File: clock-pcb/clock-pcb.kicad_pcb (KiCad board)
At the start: 2 copper layers, 66 x 42 mm, 61 parts, among them J1 Conn_01x03_Pin, J10 Conn_01x01_Socket, J11 Conn_01x01_Socket, J12 Conn_01x01_Socket, J13 Conn_01x01_Socket, J14 Conn_01x01_Socket, J15 Conn_01x02_Socket, J2 oled, J3 Led display, J4 Led display 2, J5 Conn_01x07_Socket, J6 Conn_01x07_Socket, J7 Conn_01x01_Socket, J8 Conn_01x02_Socket, J9 Conn_01x01_Socket, Q1 FS8205A, Q2 FDN304PZ, U1 ESP32-WROOM-E, U4 TPS2116DRL, U5 MCP73811T-420I-OT, U7 TLV75533PDBV

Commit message: new pcb
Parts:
- removed BATT_P1, BOOT1, EN1: TL3305AF160QG, clock:TL3305AF160QG
- removed D4: SD0805S040S0R5, Diode_SMD:D_0805_2012Metric
- removed J11, J12, J13, J14: Conn_01x01_Socket, Connector_PinSocket_2.54mm:PinSocket_1x01_P2.54mm_Vertical
- removed JP3: Jumper_bridged, Jumper:SolderJumper-2_P1.3mm_Bridged2Bar_RoundedPad1.0x1.5mm
- removed JP4: SolderJumper_3_Open, Jumper:SolderJumper-3_P1.3mm_Open_RoundedPad1.0x1.5mm
- removed Q1: FS8205A, clock:SOP65P640X120-8N
- removed Q2: FDN304PZ, Package_TO_SOT_SMD:SOT-23
- removed USB_BOARD1: Conn_01x02_Socket, clock:SHDR2W64P0X250_1X2_740X575X700P
- added C12: 1uF, Capacitor_SMD:C_0603_1608Metric, B.Cu at (93.0, 135.5)
- added C13: 1uF, Capacitor_SMD:C_0603_1608Metric, B.Cu at (99.5, 151.8)
- added C14: 1uF, Capacitor_SMD:C_0603_1608Metric, B.Cu at (98.0, 132.4)
- added C15: 1uF, Capacitor_SMD:C_0603_1608Metric, B.Cu at (106.8, 130.1)
- added C16: 4.7uF, Capacitor_SMD:C_0805_2012Metric, B.Cu at (87.5, 152.0)
- added C17: 10uF, Capacitor_SMD:C_0603_1608Metric, B.Cu at (93.9, 155.9)
- added C18: 6.4pF, Capacitor_SMD:C_0402_1005Metric, B.Cu at (92.4, 155.3)
- added C19: 19pF, Capacitor_SMD:C_0402_1005Metric, B.Cu at (91.9, 147.8)
- added C20: 19pF, Capacitor_SMD:C_0402_1005Metric, B.Cu at (91.9, 149.7)
- added C21: 1uF, Capacitor_SMD:C_0603_1608Metric, B.Cu at (89.2, 152.0)
- added C23: 0.1uF, Capacitor_SMD:C_0603_1608Metric, B.Cu at (105.0, 151.9)
- added C24: 10uF, Capacitor_SMD:C_0603_1608Metric, B.Cu at (105.0, 153.4)
- added C25: 1uF, Capacitor_SMD:C_0603_1608Metric, B.Cu at (100.8, 154.0)
- added C26: 4.7uF, Capacitor_Tantalum_SMD:CP_EIA-3528-12_Kemet-T, B.Cu at (93.3, 152.6)
- added C27: 4.7uF, Capacitor_Tantalum_SMD:CP_EIA-3528-12_Kemet-T, B.Cu at (111.5, 153.6)
- added C28: 1uF, Capacitor_SMD:C_0603_1608Metric, B.Cu at (97.6, 154.0)
- added D1: LED, LED_SMD:LED_1210_3225Metric, F.Cu at (82.9, 154.9)
- added D2: LED, LED_SMD:LED_1210_3225Metric, F.Cu at (82.9, 131.3)
- added IC2: MCP23018-E_MJ, clock:QFN50P400X400X90-25N-D, B.Cu at (90.7, 140.4)
- added JP6: Jumper, clock:jumper_solder_small, B.Cu at (99.2, 134.3)
- added L1: 10uH 1A, clock:HPI0530-100, B.Cu at (87.8, 160.0)
- added R0: 5.1k, Resistor_SMD:R_0402_1005Metric, B.Cu at (94.9, 140.5)
- added R13: 250k, Resistor_SMD:R_0402_1005Metric, B.Cu at (118.5, 135.5)
- added R14: 100k, Resistor_SMD:R_0402_1005Metric, B.Cu at (119.3, 133.6)
- added R15: 10K, Resistor_SMD:R_0402_1005Metric, B.Cu at (107.0, 126.6)
- added R16: 10K, Resistor_SMD:R_0402_1005Metric, B.Cu at (109.6, 126.6)
- added R17: 330, Resistor_SMD:R_0402_1005Metric, F.Cu at (86.2, 153.2)
- added R18: 330, Resistor_SMD:R_0402_1005Metric, F.Cu at (86.2, 156.6)
- added R19: 330, Resistor_SMD:R_0402_1005Metric, F.Cu at (86.2, 154.0)
- added R20: 330, Resistor_SMD:R_0402_1005Metric, F.Cu at (86.2, 155.8)
- added R21: 10M, Resistor_SMD:R_0402_1005Metric, B.Cu at (95.3, 148.6)
- added R22: 330, Resistor_SMD:R_0402_1005Metric, F.Cu at (86.2, 132.2)
- added R23: 330, Resistor_SMD:R_0402_1005Metric, F.Cu at (86.2, 133.0)
- added R24: 330, Resistor_SMD:R_0402_1005Metric, F.Cu at (86.2, 130.4)
- added R25: 330, Resistor_SMD:R_0402_1005Metric, F.Cu at (86.2, 129.6)
- added R26: 300k, Resistor_SMD:R_0402_1005Metric, B.Cu at (91.8, 156.9)
- added R27: 3.16M, Resistor_SMD:R_0402_1005Metric, B.Cu at (91.4, 155.3)
- added R29: 1.2M, Resistor_SMD:R_0402_1005Metric, B.Cu at (103.0, 154.0)
- added R30: 10K, Resistor_SMD:R_0402_1005Metric, B.Cu at (108.3, 153.0)
- added R31: 10K, Resistor_SMD:R_0402_1005Metric, B.Cu at (107.3, 153.0)
- added R32: N/A, Resistor_SMD:R_0402_1005Metric, B.Cu at (99.0, 136.0)
- added R33: N/A, Resistor_SMD:R_0402_1005Metric, B.Cu at (97.7, 136.0)
- added S1: TS21-34-035-BK-160-SMT-TR, clock:TS2134035BK160SMTTR, F.Cu at (142.4, 160.9)
- added S2: TS21-34-035-BK-160-SMT-TR, clock:TS2134035BK160SMTTR, F.Cu at (142.4, 155.4)
- added S5: TS21-34-035-BK-160-SMT-TR, clock:TS2134035BK160SMTTR, F.Cu at (133.5, 149.3)
- added TP1: TestPoint, TestPoint:TestPoint_THTPad_1.0x1.0mm_Drill0.5mm, F.Cu at (81.5, 127.5)
- added TP12: TestPoint, TestPoint:TestPoint_THTPad_1.0x1.0mm_Drill0.5mm, F.Cu at (90.3, 124.7)
- added TP13: TestPoint, TestPoint:TestPoint_THTPad_1.0x1.0mm_Drill0.5mm, F.Cu at (94.7, 124.7)
- added TP3: TestPoint, TestPoint:TestPoint_THTPad_1.0x1.0mm_Drill0.5mm, F.Cu at (83.6, 124.7)
- added TP4: TestPoint, TestPoint:TestPoint_THTPad_1.0x1.0mm_Drill0.5mm, F.Cu at (81.4, 124.7)
- added TP5: TestPoint, TestPoint:TestPoint_THTPad_1.0x1.0mm_Drill0.5mm, F.Cu at (88.0, 124.7)
- added TP6: TestPoint, TestPoint:TestPoint_THTPad_1.0x1.0mm_Drill0.5mm, F.Cu at (85.8, 124.7)
- added TP7: TestPoint, TestPoint:TestPoint_THTPad_1.0x1.0mm_Drill0.5mm, F.Cu at (92.5, 124.7)
- added TP8: TestPoint, TestPoint:TestPoint_THTPad_1.0x1.0mm_Drill0.5mm, F.Cu at (96.9, 124.7)
- added TP9: TestPoint, TestPoint:TestPoint_THTPad_1.0x1.0mm_Drill0.5mm, F.Cu at (83.8, 127.5)
- added U6: TPS61040DBV, Package_TO_SOT_SMD:SOT-23-5, B.Cu at (88.6, 155.7)
- added U8: AT42QT2120-MMHR, clock:QFN45P300X300X85-21N, B.Cu at (102.1, 129.4)
- added Y2: 32.768KHz, clock:XTAL_9HT10_TXC, B.Cu at (93.6, 148.6)
- C1: value 22uF -> 0.1uF; footprint Capacitor_SMD:C_0805_2012Metric -> Capacitor_SMD:C_0603_1608Metric
- C10, C11, U5: moved to B.Cu
- C3: value 0.1uF -> 10uF
- D3: value SD0805S040S0R5 -> NSVR0340HT1G; footprint Diode_SMD:D_0805_2012Metric -> Diode_SMD:D_SOD-323
- J10: value Conn_01x01_Socket -> Conn_01x05_Socket; footprint Connector_PinSocket_2.54mm:PinSocket_1x01_P2.54mm_Vertical -> Connector_PinHeader_2.54mm:PinHeader_1x05_P2.54mm_Vertical
- J2: value oled -> oled 2
- J5, J6: footprint Connector_PinSocket_2.54mm:PinSocket_1x07_P2.54mm_Vertical -> Connector_PinHeader_2.54mm:PinHeader_1x07_P2.54mm_Vertical
- J7: value Conn_01x01_Socket -> SFV25R-2STE1HLF; footprint Connector_PinSocket_2.54mm:PinSocket_1x01_P2.54mm_Vertical -> clock:OLED_1.5IN_128X128MONO; moved to F.Cu
- J8: value Conn_01x02_Socket -> SFV25R-2STE1HLF; footprint Connector_PinSocket_2.54mm:PinSocket_1x02_P2.54mm_Vertical -> clock:AMPHENOL_SFV25R-2STE1HLF
- J9: value Conn_01x01_Socket -> Conn_01x04_Socket; footprint Connector_PinSocket_2.54mm:PinSocket_1x01_P2.54mm_Vertical -> Connector_JST:JST_XH_B4B-XH-AM_1x04_P2.50mm_Vertical
- JP1, JP7: footprint Jumper:SolderJumper-2_P1.3mm_Open_RoundedPad1.0x1.5mm -> clock:jumper_solder_small
- JP2: value Jumper -> SolderJumper_3_Bridged12; footprint Jumper:SolderJumper-2_P1.3mm_Open_RoundedPad1.0x1.5mm -> clock:jumper_solder_small_3_bridged
- JP5: value SolderJumper_2_Open -> Jumper; footprint Jumper:SolderJumper-2_P1.3mm_Open_RoundedPad1.0x1.5mm -> clock:jumper_solder_small; moved to B.Cu
- R1: value 10k -> 100k
- R10: value 800k -> 10K
- R11: value 5.1k -> 10K
- R12: value 5.1k -> 100k
- R7: value 500k -> 47K
- R8: value 100K -> 10K
- R9: value 50k -> 10K
- U1: value ESP32-WROOM-E -> ESP32-C6-MINI-1-N4; footprint PCM_Espressif:ESP32-WROOM-32E -> clock:XCVR_ESP32-C6-MINI-1-N4
- U3: footprint clock:SHDR2W64P0X250_1X2_740X575X700P -> Connector_JST:JST_XH_B2B-XH-AM_1x02_P2.50mm_Vertical
- moved J8 37.8 mm to (104.5, 158.7), turned to 180 degrees
- moved J9 29.8 mm to (122.9, 146.8)
- moved C1 28.6 mm to (105.1, 130.1), turned to 90 degrees
- moved D3 28.0 mm to (92.5, 159.4)
- moved R8 25.4 mm to (99.4, 126.6), turned to -90 degrees
- moved R10 25.2 mm to (105.0, 126.6)
- moved R9 24.6 mm to (102.9, 126.3), turned to -90 degrees
- moved R7 23.8 mm to (98.9, 131.0), turned to 0 degrees
- moved JP5 22.7 mm to (97.4, 134.3), turned to 0 degrees
- moved R1 22.3 mm to (106.0, 134.7), turned to 90 degrees
- moved C2 20.4 mm to (89.8, 135.5), turned to 90 degrees
- moved JP2 19.7 mm to (101.2, 126.3), turned to 180 degrees
- moved R11 17.8 mm to (101.9, 152.1), turned to 180 degrees
- moved C3 17.2 mm to (91.3, 135.5), turned to 90 degrees
- moved J7 16.6 mm to (104.5, 144.4), turned to 0 degrees
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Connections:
- net CO renamed Net-(AO9926C1-G2)
- net DO renamed Net-(AO9926C1-G1)
- C1 pad 1: +3V3 -> GND
- C1 pad 2: GND -> +3V3
- C3 pad 1: GND -> +3V3
- C3 pad 2: EN -> GND
- D3 pad 1: Net-(D3-K) -> 14V_OLED
- D3 pad 2: VBUS -> Net-(D3-A)
- J2 pad 1: +3V3 -> GND
- J2 pad 2: GND -> +3V3
- J3 pad 1: CLK -> SCL
- J3 pad 2: DIO -> SDA
- J4 pad 1: GND -> CLK
- J4 pad 2: +3V3 -> DIO
- J4 pad 3: DIO -> GND
- J4 pad 4: CLK -> +3V3
- J5 pad 3: GPIO35 -> SUB_TOP_3
- J5 pad 4: GPIO14 -> BUZZER
- J5 pad 5: GPIO15 -> SUB_TOP_1
- J6 pad 3: GPIO39 -> HALL_SENS
- J6 pad 4: GPIO26 -> BUTTON_EXIT
- J6 pad 5: GPIO25 -> BUTON_CONF
- J7 pad 1: Net-(J7-Pin_1) -> GND
- J8 pad 2: GPIO4_T -> 14V_OLED
- J9 pad 1: Net-(J9-Pin_1) -> GND
- JP2 pad 1: GND -> Net-(JP2-A)
- JP2 pad 2: Net-(JP2-B) -> GUARD
- JP5 pad 1: GND -> SDA
- JP5 pad 2: CHARGE_EN -> MOSI
- R1 pad 2: EN -> SCL
- R10 pad 1: POWER_STATUS -> Net-(J10-Pin_3)
- R10 pad 2: GND -> SLID_1
- R11 pad 2: SCL -> EN
- R2 pad 2: ADC_BATT -> ADC
- R3 pad 1: ADC_BATT -> ADC
- R7 pad 1: VBUS -> +3V3
- R7 pad 2: POWER_STATUS -> TOUCH_INT
- R8 pad 1: Net-(D3-K) -> Net-(J10-Pin_5)
- R8 pad 2: GND -> SLID_0
- R9 pad 1: VBUS -> Net-(J10-Pin_4)
- R9 pad 2: GND -> GUARD
- S3 pad 1: GND -> +3V3
- S3 pad 2: GND -> +3V3
- S4 pad 1: GND -> +3V3
- S4 pad 2: GND -> +3V3
- U1 pad 10: GPIO25 -> INT_A
- U1 pad 11: GPIO26 -> GND
- U1 pad 12: Net-(J11-Pin_1) -> CLOCK_P
- U1 pad 13: GPIO14 -> CLOCK_N
- U1 pad 14: BUTTON_UP -> GND
- U1 pad 15: GND -> SDA
- U1 pad 16: BUTTON_DOWN -> SCL
- U1 pad 17: (no net) -> DN
- U1 pad 18: (no net) -> DP
- U1 pad 19: (no net) -> CLK
- U1 pad 2: +3V3 -> GND
- U1 pad 20: (no net) -> DIO
- U1 pad 21: (no net) -> unconnected-(U1-NC__2-Pad21)
- U1 pad 22: (no net) -> Net-(U1-IO8)
- U1 pad 23: GPIO15 -> GPIO9
- U1 pad 24: Net-(J10-Pin_1) -> BUZZER
- U1 pad 25: IO0 -> Net-(U1-IO19)
- U1 pad 26: GPIO4_T -> Net-(U1-IO20)
- U1 pad 27: Net-(J12-Pin_1) -> DC
- U1 pad 28: Net-(J13-Pin_1) -> CS
- U1 pad 29: Net-(J9-Pin_1) -> Net-(U1-IO23)
- U1 pad 3: EN -> +3V3
- U1 pad 30: CLK -> RX
- U1 pad 31: DIO -> TX
- U1 pad 32: (no net) -> unconnected-(U1-NC__3-Pad32)
- U1 pad 33: SDA -> unconnected-(U1-NC__4-Pad33)
- U1 pad 34: RX -> unconnected-(U1-NC__5-Pad34)
- U1 pad 35: TX -> unconnected-(U1-NC__6-Pad35)
- U1 pad 36: SCL -> GND
- U1 pad 37: CHARGE_EN -> GND
- U1 pad 4: POWER_STATUS -> unconnected-(U1-NC-Pad4)
- U1 pad 5: GPIO39 -> Net-(U1-IO2)
- U1 pad 6: ADC_BATT -> TOUCH_INT
- U1 pad 7: GPIO35 -> unconnected-(U1-NC__1-Pad7)
- U1 pad 8: Net-(J7-Pin_1) -> EN
- U1 pad 9: Net-(J14-Pin_1) -> ADC
- U4 pad 4: Net-(JP2-B) -> Net-(U4-PR1)
- U5 pad 5: Net-(JP4-C) -> GND
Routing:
- net +3V3: track 112.3 -> 0.00 mm, vias 2 -> 0
- net SCL: track 112.2 -> 0.00 mm, vias 2 -> 0
- net SDA: track 97.0 -> 0.00 mm, vias 1 -> 0
- net GPIO35: track 65.5 -> 0.00 mm
- net GPIO39: track 61.0 -> 0.00 mm, vias 1 -> 0
- net GPIO25: track 55.6 -> 0.00 mm, vias 1 -> 0
- net GPIO26: track 54.3 -> 0.00 mm, vias 1 -> 0
- net POWER_STATUS: track 50.5 -> 0.00 mm
- net GPIO14: track 49.9 -> 0.00 mm, vias 2 -> 0
- net BUTTON_UP: track 49.5 -> 0.00 mm, vias 1 -> 0
- net GND: track 48.2 -> 0.00 mm, vias 202 -> 0
- net BUTTON_DOWN: track 46.1 -> 0.00 mm, vias 2 -> 0
- net LDO_IN: track 44.5 -> 0.00 mm
- net +BATT: track 43.4 -> 0.00 mm, vias 1 -> 0
- net Net-(J9-Pin_1): track 38.0 -> 0.00 mm, vias 3 -> 0
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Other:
- outline, holes or cut-outs redrawn
- board text removed: "GPIO16"
- board text removed: "GPIO17"
- board text removed: "GPIO2"
- board text removed: "GPIO27"
- board text removed: "GPIO32"
- board text removed: "GPIO33"
- board text removed: "GPIO4_T"
- board text removed: "GPIO5"

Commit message: routing
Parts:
- R2, R3, S5: moved to B.Cu
- moved R2 5.06 mm to (117.5, 152.7)
- moved R3 5.06 mm to (115.5, 152.7)
- moved TP8 4.45 mm to (92.5, 124.7)
- moved TP12 4.44 mm to (94.7, 124.7)
- moved TP3 2.24 mm to (81.4, 124.7)
- moved TP5 2.24 mm to (85.8, 124.7)
- moved TP7 2.23 mm to (90.3, 124.7)
- moved TP13 2.22 mm to (96.9, 124.7)
- moved TP6 2.21 mm to (88.0, 124.7)
- moved TP4 2.21 mm to (83.6, 124.7)
- moved S2 1.03 mm to (143.4, 155.6)
- moved S1 1.03 mm to (143.4, 161.1)
- moved JP1 0.40 mm to (128.4, 155.0)
- moved J8 0.40 mm to (104.5, 159.1)
- moved R14 0.25 mm to (119.1, 133.8)
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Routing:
- net +3V3: track 0.00 -> 253.5 mm, vias 0 -> 9
- net GND: track 0.00 -> 155.3 mm, vias 0 -> 127
- net SDA: track 0.00 -> 133.0 mm, vias 0 -> 6
- net EN: track 0.00 -> 128.3 mm, vias 0 -> 11
- net SCL: track 0.00 -> 122.0 mm, vias 0 -> 4
- net SUB_TOP_1: track 0.00 -> 114.5 mm, vias 0 -> 6
- net SUB_TOP_3: track 0.00 -> 112.7 mm, vias 0 -> 6
- net GPIO9: track 0.00 -> 73.4 mm, vias 0 -> 3
- net BUTTON_EXIT: track 0.00 -> 69.3 mm, vias 0 -> 3
- net BUTTON_DOWN: track 0.00 -> 58.6 mm, vias 0 -> 3
- net BUTON_CONF: track 0.00 -> 56.2 mm, vias 0 -> 1
- net BUZZER: track 0.00 -> 56.1 mm, vias 0 -> 2
- net BUTTON_UP: track 0.00 -> 53.4 mm, vias 0 -> 3
- net TOUCH_INT: track 0.00 -> 51.9 mm, vias 0 -> 4
- net Net-(U1-IO2): track 0.00 -> 50.2 mm, vias 0 -> 2
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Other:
- outline, holes or cut-outs redrawn
- board text added: "BOOT"
- board text added: "EN"
- board text removed: "3.3V"
- board text removed: "GND"

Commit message: touch slider pcb
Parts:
- removed J10: Conn_01x05_Socket, Connector_PinHeader_2.54mm:PinHeader_1x05_P2.54mm_Vertical
- added J11: Conn_01x06_Socket, Connector_PinHeader_2.54mm:PinHeader_1x06_P2.54mm_Vertical, B.Cu at (112.1, 124.2)
- added R28: 10K, Resistor_SMD:R_0402_1005Metric, B.Cu at (139.8, 149.3)
- moved R15 34.2 mm to (139.8, 136.6)
- moved TP12 0.49 mm to (94.7, 124.2)
- moved TP13 0.49 mm to (96.9, 124.2)
- moved TP3 0.49 mm to (81.4, 124.2)
- moved TP4 0.49 mm to (83.6, 124.2)
- moved TP5 0.49 mm to (85.8, 124.2)
- moved TP6 0.49 mm to (88.0, 124.2)
- moved TP7 0.49 mm to (90.3, 124.2)
- moved TP8 0.49 mm to (92.5, 124.2)
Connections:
- JP2 pad 1: Net-(JP2-A) -> GUARD
- R15 pad 1: Net-(J10-Pin_2) -> BUTTON_UP
- R15 pad 2: GUARD -> +3V3
- R16 pad 2: SLID_1 -> SLID_0
- R8 pad 2: SLID_0 -> SLID_2
- S3 pad 1: +3V3 -> GND
- S3 pad 2: +3V3 -> GND
- S4 pad 1: +3V3 -> GND
- S4 pad 2: +3V3 -> GND
- U8 pad 4: Net-(JP2-A) -> GUARD
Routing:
- net GND: track 155.3 -> 189.2 mm, vias 127 -> 131
- net +3V3: track 253.5 -> 222.2 mm, vias 9 -> 11
- net Net-(J11-Pin_1): track 1.80 -> 13.2 mm
- net SLID_1: track 8.45 -> 1.99 mm, vias 2 -> 0
- net SLID_2: track 0.00 -> 6.31 mm, vias 0 -> 2
- net SLID_0: track 11.0 -> 6.75 mm, vias 2 -> 0
- net SCL: track 122.0 -> 119.9 mm
- net BUTTON_UP: track 53.4 -> 55.5 mm
- net Net-(JP2-A): track 1.94 -> 0.00 mm
- net BUTTON_DOWN: track 58.6 -> 60.4 mm
- net Net-(J10-Pin_2): track 1.74 -> 0.00 mm
- net GUARD: track 7.67 -> 6.90 mm
- net SDA: track 133.0 -> 132.4 mm
- net Net-(U8-KEY4/GPO2): track 7.71 -> 8.22 mm

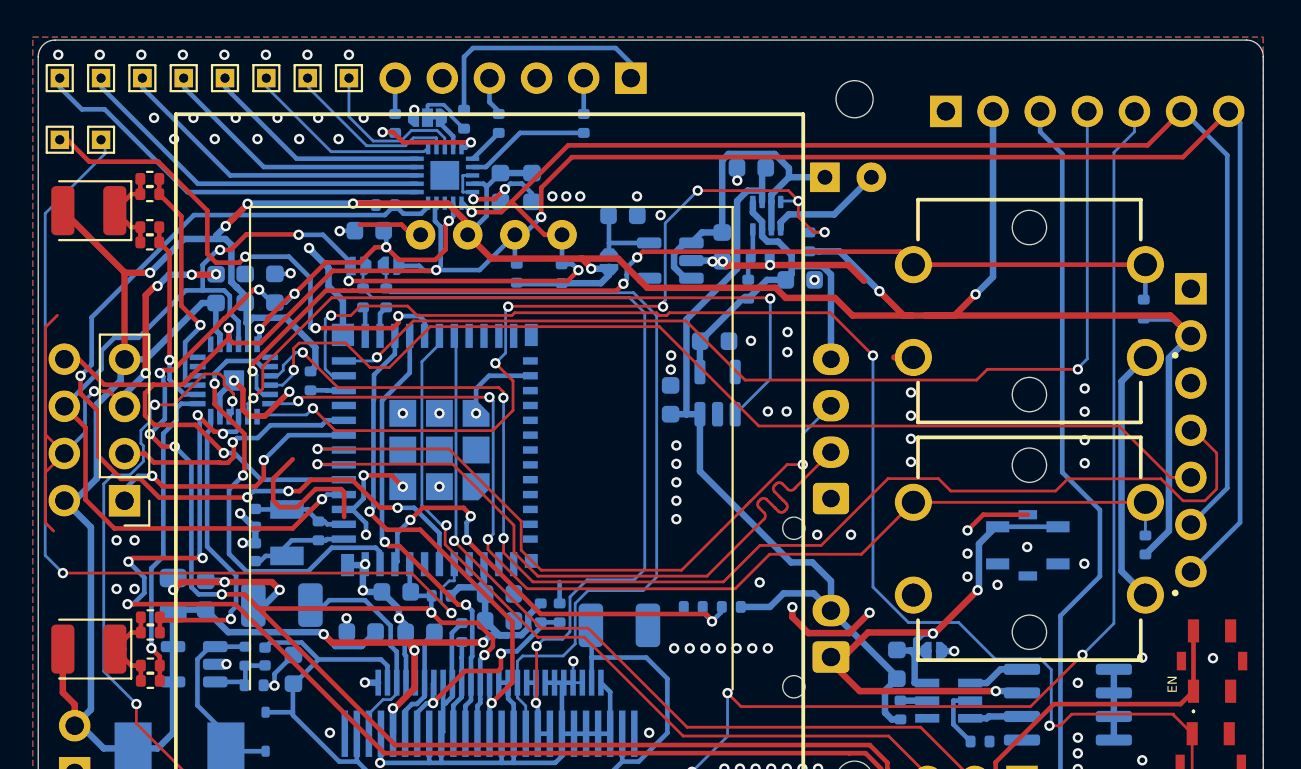
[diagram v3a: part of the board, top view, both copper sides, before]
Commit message: voltage regulator
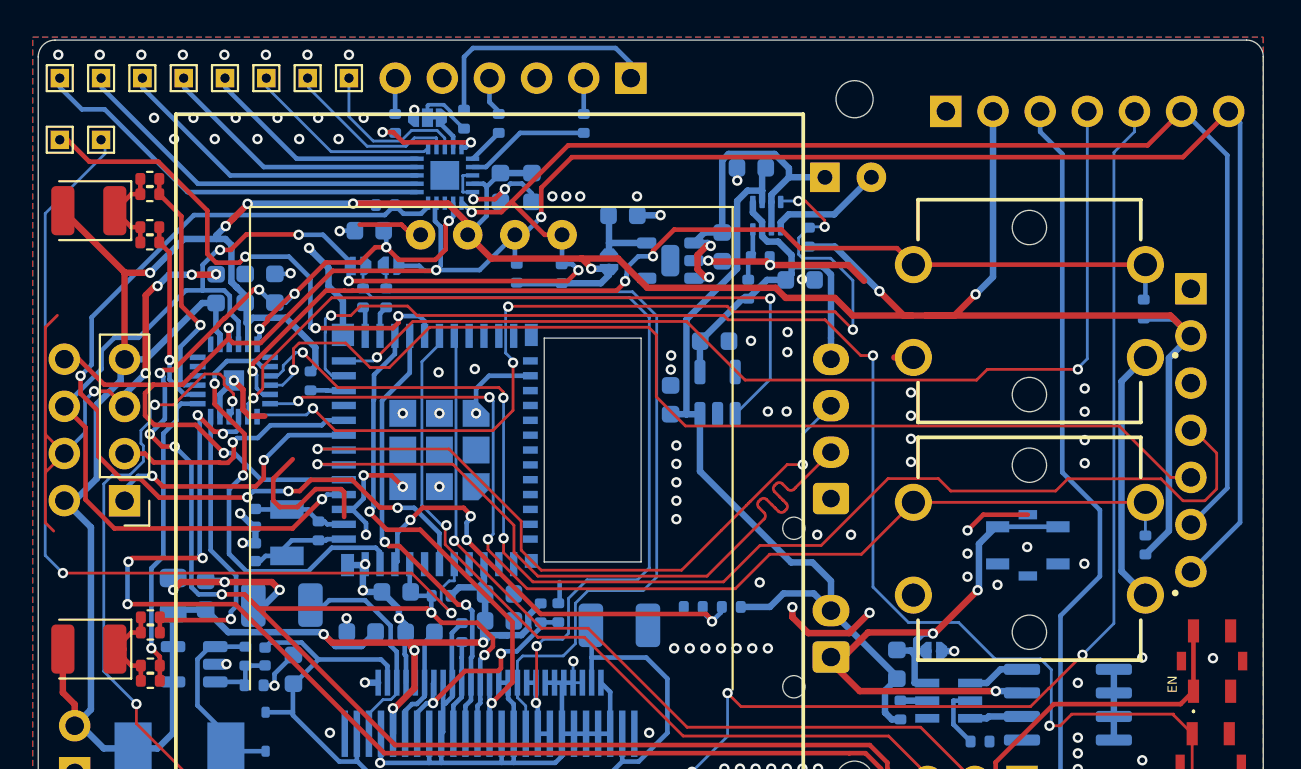
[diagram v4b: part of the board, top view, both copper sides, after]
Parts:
- U7: footprint Package_TO_SOT_SMD:SOT-23-5 -> clock:TLV75733PDYDR
- moved R6 0.26 mm to (121.7, 132.7)
- moved R30 0.07 mm to (108.2, 153.0)
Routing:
- net POWER_STATUS: track 46.7 -> 51.7 mm, vias 7 -> 6
- net BUTON_CONF: track 56.2 -> 58.1 mm
- net BUTTON_UP: track 55.5 -> 56.7 mm
- net LDO_IN: track 18.5 -> 19.6 mm, vias 0 -> 2
- net SUB_TOP_3: track 112.7 -> 111.9 mm
- net GND: track 189.2 -> 189.3 mm, vias 131 -> 127
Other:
- outline, holes or cut-outs redrawn

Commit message: panel
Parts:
- added C22: 6.4pF, Capacitor_SMD:C_01005_0402Metric, B.Cu at (93.4, 155.5)
- added TP10: TestPoint, TestPoint:TestPoint_THTPad_1.0x1.0mm_Drill0.5mm, F.Cu at (85.8, 127.5)
- added TP2: TestPoint, TestPoint:TestPoint_Pad_D1.0mm, B.Cu at (93.8, 161.4)
- J4: footprint Connector_PinHeader_2.54mm:PinHeader_1x04_P2.54mm_Vertical -> clock:PinHeader_1x04_P2.54mm_Vertical
- moved C5 0.97 mm to (123.6, 129.6)
- moved C17 0.76 mm to (94.7, 156.0)
- moved R26 0.20 mm to (91.8, 157.1)
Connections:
- IC2 pad 13: unconnected-(IC2-INTB-Pad13) -> INT_A
- IC2 pad 4: unconnected-(IC2-GPB4-Pad4) -> HALL_SENS
- IC2 pad 6: unconnected-(IC2-GPB6-Pad6) -> Net-(IC2-GPB6)
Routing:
- net HALL_SENS: track 0.00 -> 102.6 mm, vias 0 -> 5
- net Net-(IC2-GPB6): track 0.00 -> 21.5 mm, vias 0 -> 1
- net GND: track 189.3 -> 195.0 mm, vias 127 -> 307
- net 14V_OLED: track 48.5 -> 51.7 mm
- net SUB_TOP_1: track 114.5 -> 112.9 mm
- net Net-(U6-FB): track 3.80 -> 4.96 mm
- net LDO_IN: track 19.6 -> 20.6 mm
- net EN: track 128.8 -> 129.8 mm, vias 11 -> 10
- net LED2_P2: track 13.3 -> 12.5 mm
- net INT_A: track 23.9 -> 24.4 mm

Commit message: not compiling yet
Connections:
- R27 pad 1: Net-(D3-A) -> 14V_OLED
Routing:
- net Net-(D3-A): track 10.7 -> 9.03 mm
- net 14V_OLED: track 51.7 -> 52.7 mm
